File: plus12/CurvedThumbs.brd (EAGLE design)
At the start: 123.8 x 54 mm, 14 parts

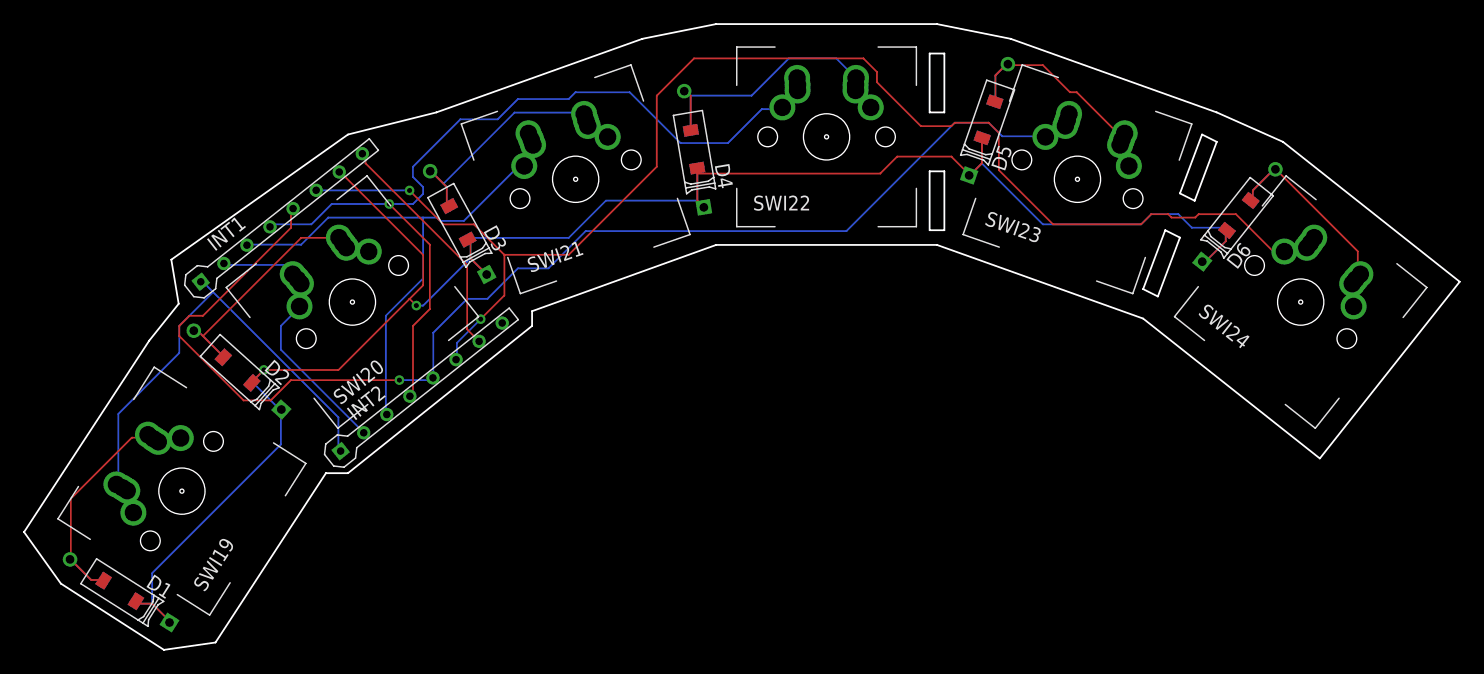
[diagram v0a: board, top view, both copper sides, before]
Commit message: Adding straight thumbs, using Othermill DRCs
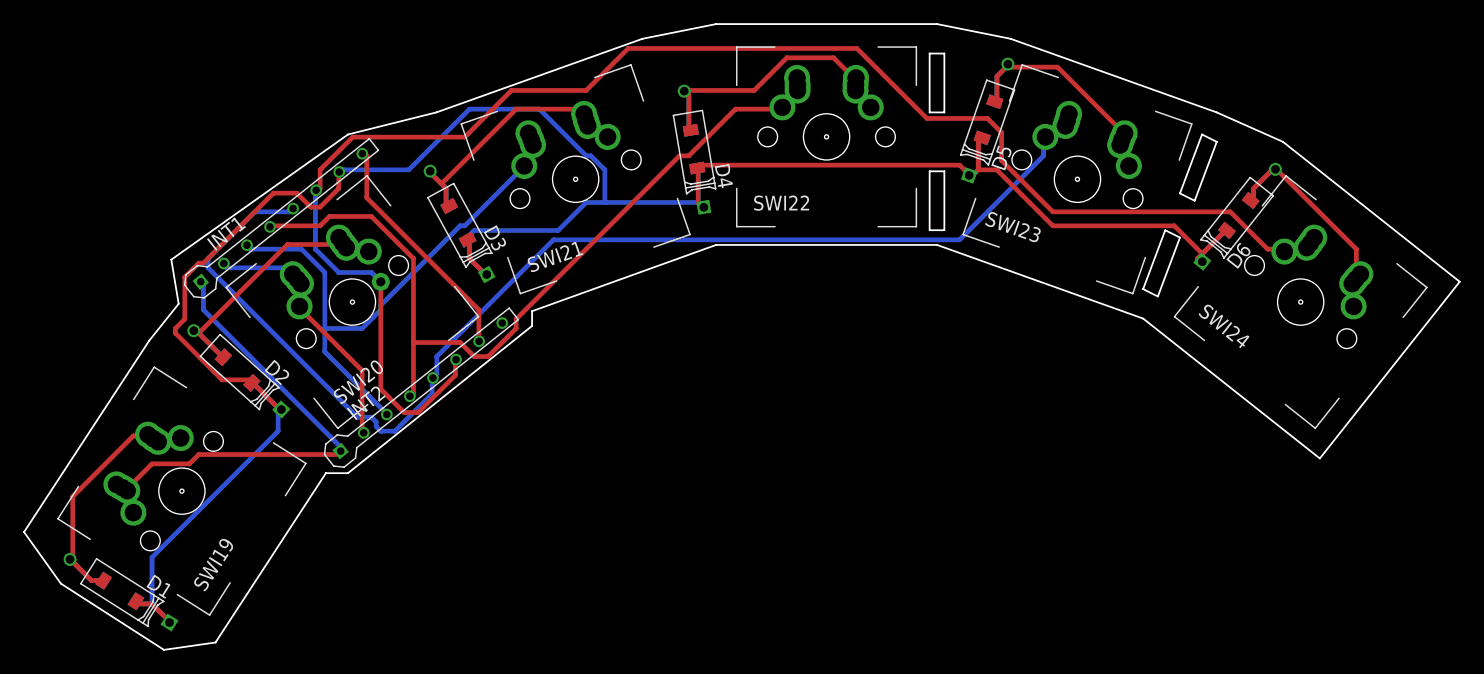
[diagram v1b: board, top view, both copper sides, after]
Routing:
- net N$13: track 171.9 -> 197.9 mm, vias 2 -> 0
- net N$12: track 121.9 -> 133.6 mm, vias 2 -> 1
- net N$10: track 77.5 -> 72.4 mm, vias 1 -> 0
- net N$11: track 108.8 -> 106.0 mm, vias 1 -> 0
- net N$2: track 22.5 -> 23.8 mm
- net N$7: track 44.0 -> 44.9 mm
- net N$8: track 24.7 -> 24.1 mm

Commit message: Kobe beefing it up
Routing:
- net N$11: track 106.0 -> 138.0 mm
- net N$12: track 133.6 -> 112.1 mm
- net N$13: track 197.9 -> 205.5 mm
- net N$10: track 72.4 -> 74.5 mm
- net N$8: track 24.1 -> 25.5 mm
- net N$7: track 44.9 -> 44.1 mm
- net N$3: track 22.4 -> 23.0 mm
- net N$5: track 20.8 -> 21.4 mm

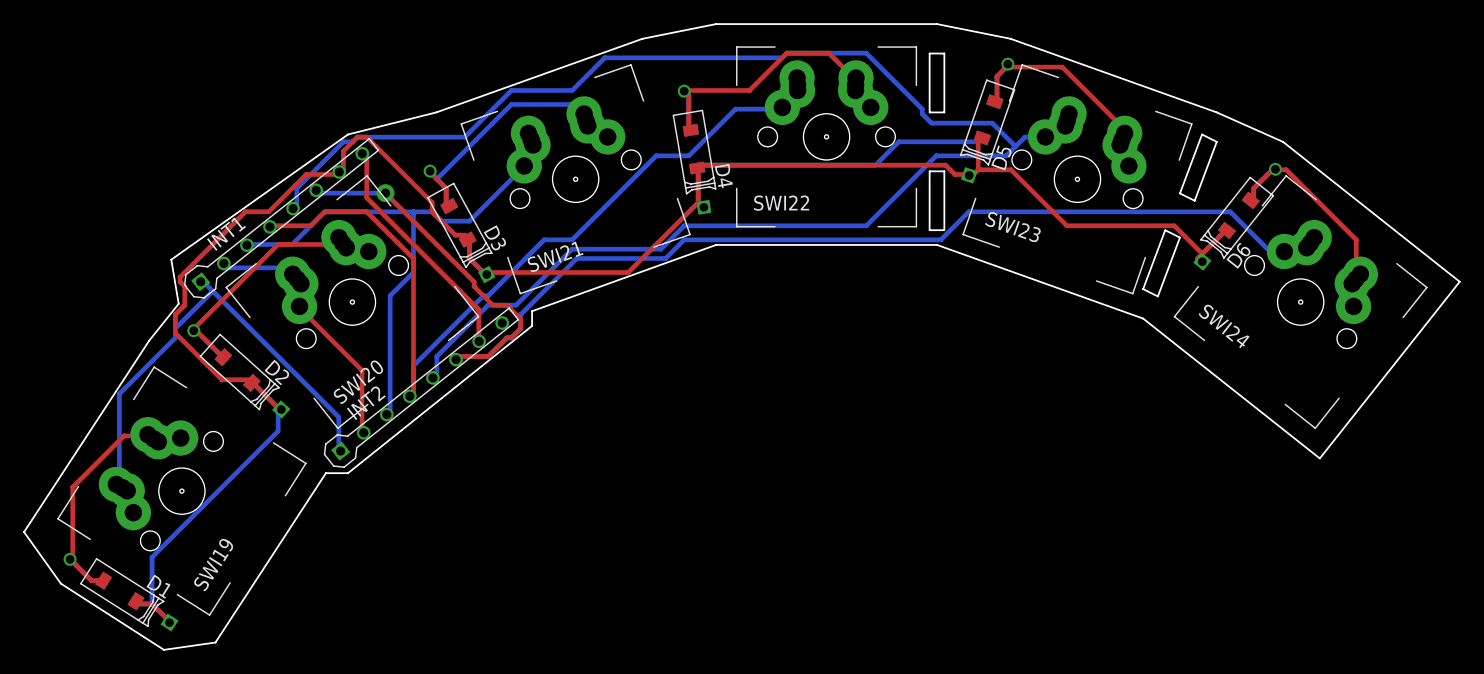
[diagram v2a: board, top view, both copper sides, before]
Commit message: Updating library pad sizes
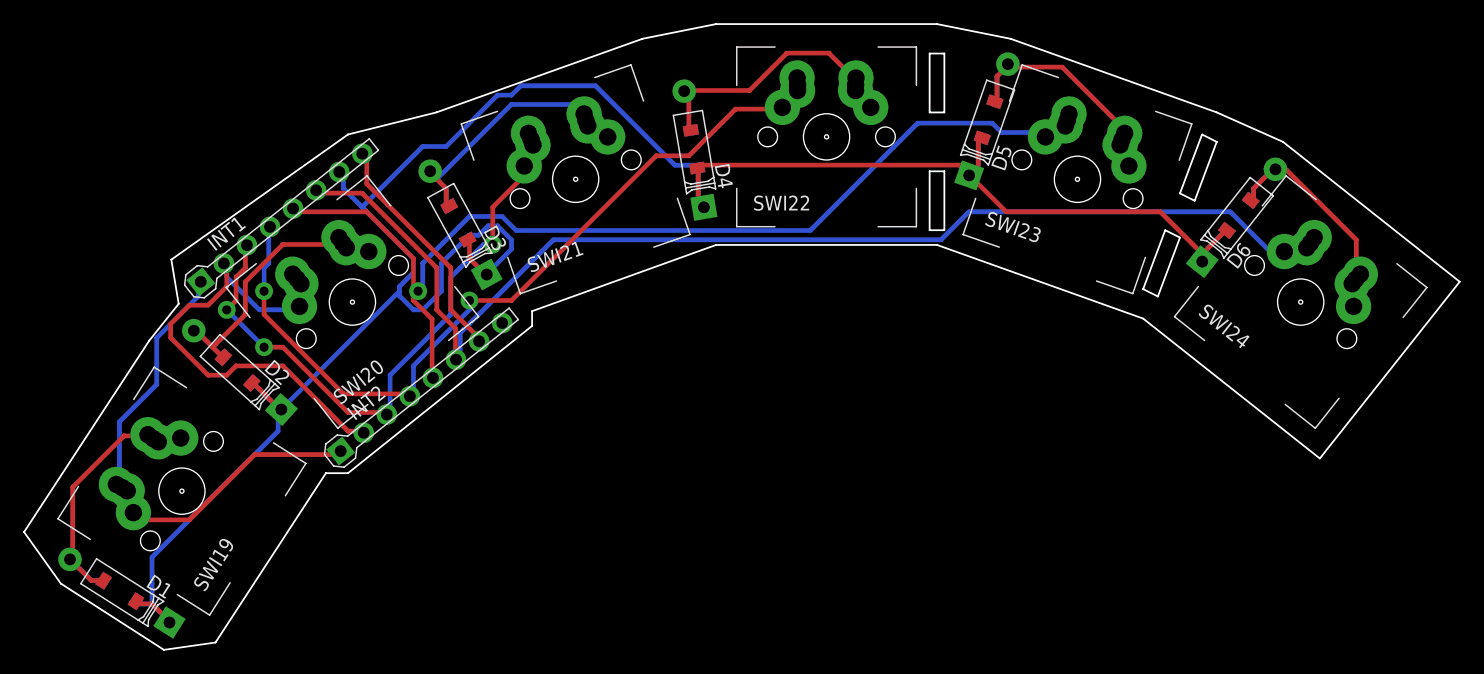
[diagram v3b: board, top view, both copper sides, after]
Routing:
- net N$11: track 138.0 -> 90.1 mm, vias 0 -> 1
- net N$8: track 25.5 -> 43.4 mm
- net N$13: track 205.5 -> 193.7 mm
- net N$12: track 112.1 -> 105.3 mm, vias 1 -> 0
- net N$9: track 50.2 -> 54.5 mm, vias 0 -> 3
- net N$10: track 74.5 -> 71.6 mm, vias 0 -> 2
- net N$7: track 44.1 -> 46.7 mm
- net N$3: track 23.0 -> 23.9 mm
- net N$2: track 23.5 -> 24.2 mm

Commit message: Updates, BEFORE C5/6 Move
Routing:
- net N$13: track 193.7 -> 194.7 mm
- net N$4: track 24.3 -> 25.2 mm
- net N$10: track 71.6 -> 70.9 mm
